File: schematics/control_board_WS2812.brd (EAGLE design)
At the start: 58.4 x 55.9 mm, 48 parts, among them J1 POWER_JACKPTH, U1 ATMEGA168, Y1 16MHZ

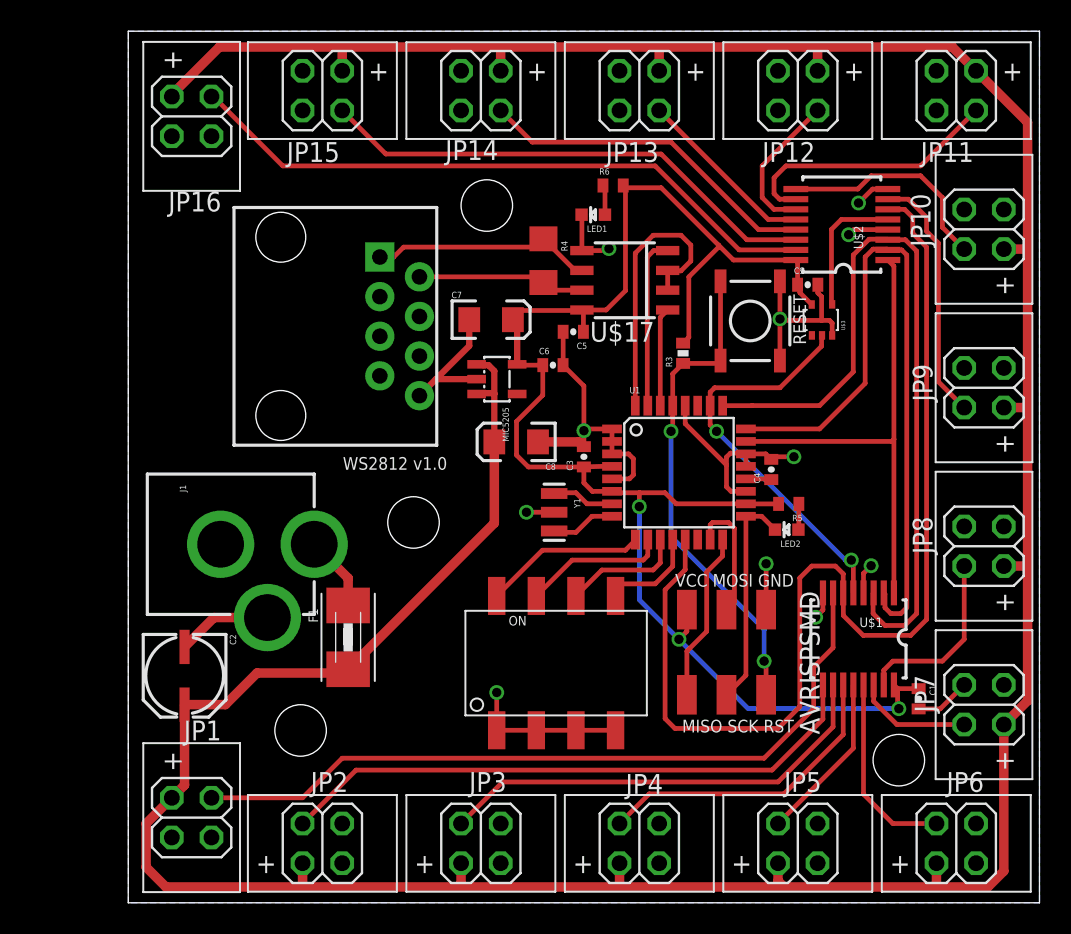
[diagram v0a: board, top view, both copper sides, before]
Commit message: changed WS2812 controller to uUSB, minor spacing edits to everything else
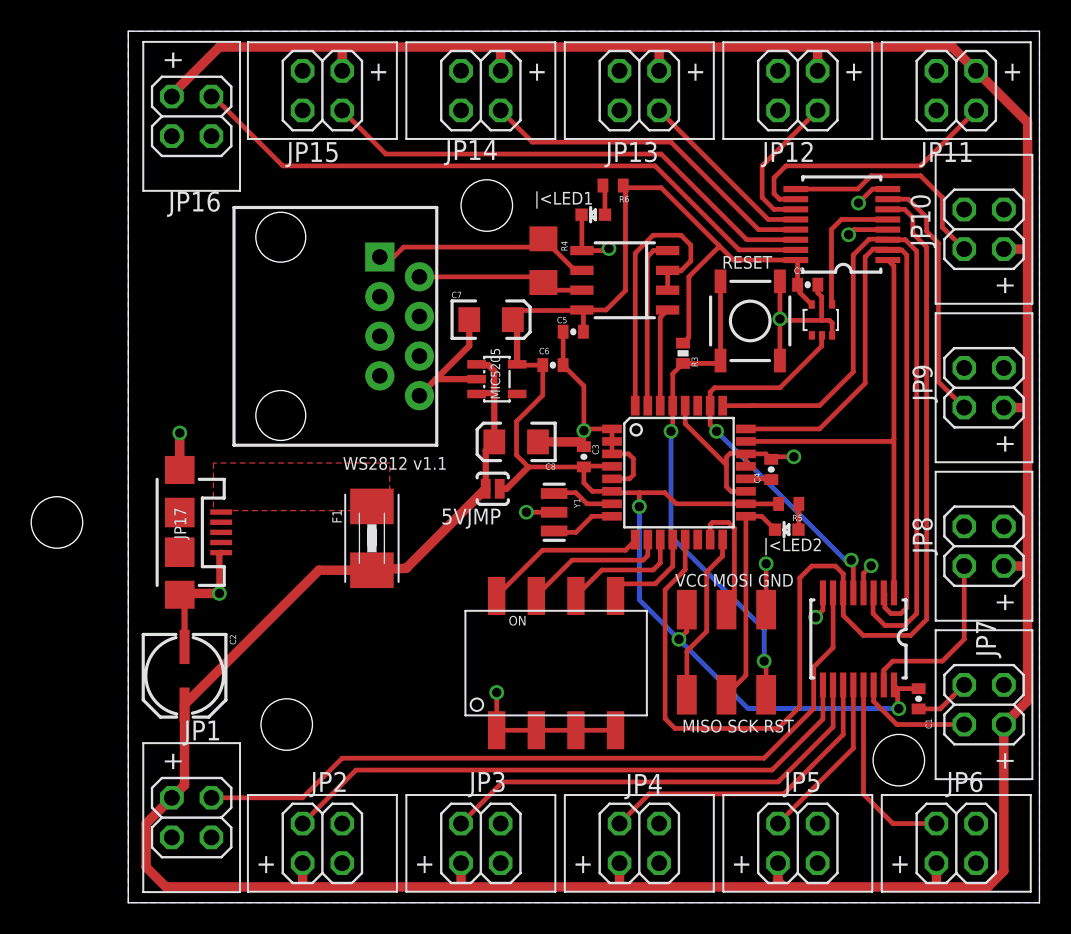
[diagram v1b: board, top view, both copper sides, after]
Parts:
- removed J1: POWER_JACKPTH, SparkFun-Connectors:POWER_JACK_PTH
- added 5VJMP: (no value), SparkFun-Passives:SJ_2S-NO
- added JP17: USB-MICROB, SparkFun-Connectors:USB-MICROB
- moved STANDOFF4 22.9 mm to (-4.32, 24.4)
- moved F1 6.53 mm to (15.9, 23.4)
- moved STANDOFF3 0.97 mm to (10.4, 11.4)
- renumbered LED1 to |<LED1, LED2 to |<LED2
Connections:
- net GND: now also JP17.GND, JP17.MT1, JP17.MT2; no longer J1.GND, J1.GNDBREAK
- net N$8: now also JP17.VBUS; no longer J1.PWR
- net VCC: now also 5VJMP.2
- net VDD: now also 5VJMP.1
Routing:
- net GND: track 90.3 -> 95.3 mm, vias 11 -> 13
- net N$8: track 4.82 -> 0.00 mm
- net VCC: track 102.7 -> 105.1 mm
- net VDD: track 230.0 -> 228.3 mm
- added copper zone on layer 1, net N$8
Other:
- board text added: "WS2812 v1.1"
- board text removed: "WS2812 v1.0"

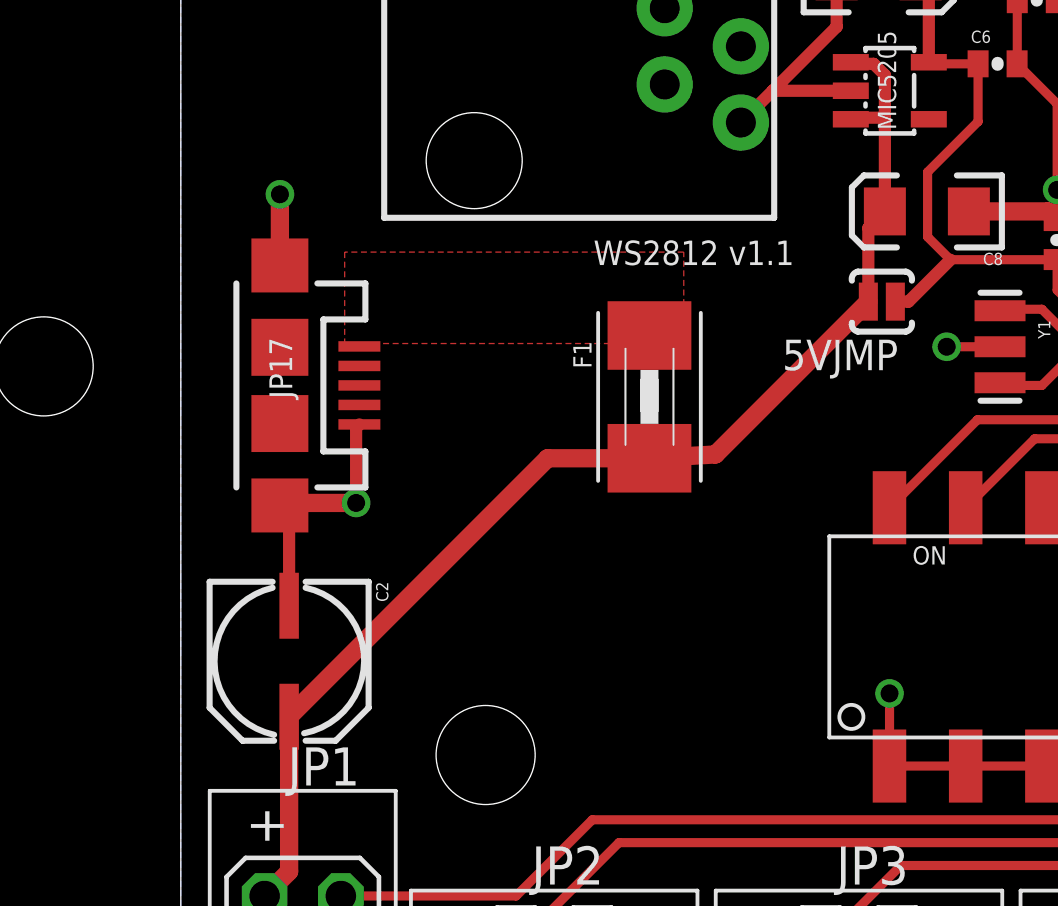
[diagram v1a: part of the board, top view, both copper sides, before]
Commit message: added full ethernet switch board (unfinished), modified WS2812 controller
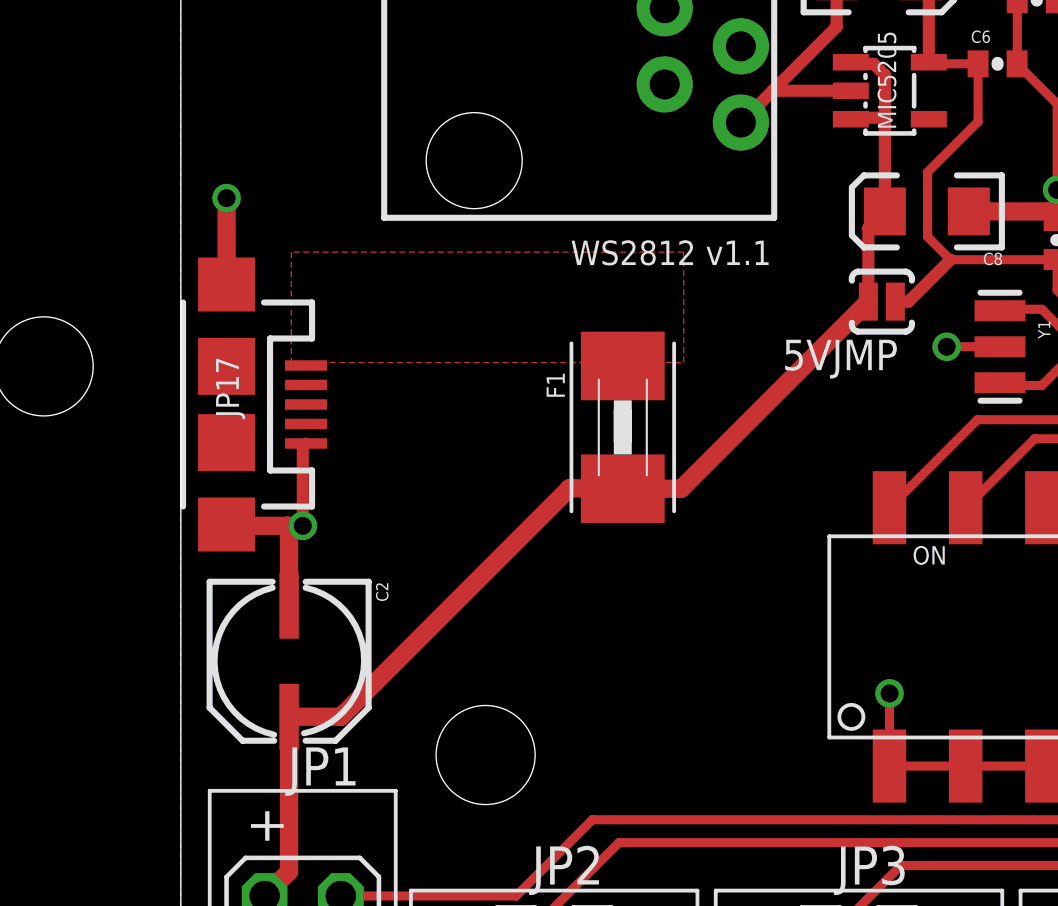
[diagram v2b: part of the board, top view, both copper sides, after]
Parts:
- moved JP17 1.89 mm to (1.78, 23.1)
- moved F1 1.35 mm to (15.0, 22.4)
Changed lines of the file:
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@@
 <wire x1="58.674" y1="55.88" x2="0.254" y2="55.88" width="0" layer="20"/>
 <wire x1="0.254" y1="55.88" x2="0.254" y2="0" width="0" layer="20"/>
-<text x="20.701" y="28.575" size="0.8128" layer="21" ratio="20" distance="213" align="top-right">WS2812 v1.1</text>
+<text x="19.939" y="28.575" size="0.8128" layer="21" ratio="20" distance="213" align="top-right">WS2812 v1.1</text>
 <text x="42.926" y="21.082" size="0.8128" layer="25" ratio="15" distance="130" rot="R180">VCC MOSI GND
 MISO SCK RST</text>
@@
 <attribute name="VALUE" x="43.48660625" y="25.00281875" size="0.4064" layer="27" rot="R180"/>
 </element>
-<element name="F1" library="adafruit" package="1812" value="" x="15.875" y="23.368" rot="R270"/>
+<element name="F1" library="adafruit" package="1812" value="" x="14.986" y="22.352" rot="R270"/>
 <element name="STANDOFF3" library="SparkFun-Electromechanical" package="STAND-OFF" value="STAND-OFF" x="10.414" y="11.43"/>
 <element name="JP1" library="pinhead" package="2X02" value="" x="4.318" y="5.461" smashed="yes" rot="R90">
@@
 <attribute name="VALUE" x="46.303940625" y="34.6950375" size="0.254" layer="27" rot="R90"/>
 </element>
-<element name="JP17" library="SparkFun-Connectors" package="USB-MICROB" value="USB-MICROB" x="3.556" y="23.749" rot="R270">
-<attribute name="PROD_ID" value="CONN-09505" x="3.556" y="23.749" size="1.778" layer="27" rot="R270" display="off"/>
+<element name="JP17" library="SparkFun-Connectors" package="USB-MICROB" value="USB-MICROB" x="1.778" y="23.114" rot="R270">
+<attribute name="PROD_ID" value="CONN-09505" x="1.778" y="23.114" size="1.778" layer="27" rot="R270" display="off"/>
 </element>
 <element name="5VJMP" library="SparkFun-Passives" package="SJ_2S-NO" value="" x="23.622" y="26.543" smashed="yes">
@@
 <contactref element="JP17" pad="MT2"/>
 <contactref element="JP17" pad="MT1"/>
-<wire x1="3.864" y1="16.405" x2="3.864" y2="19.441" width="0.4064" layer="1"/>
-<wire x1="3.864" y1="19.441" x2="3.556" y2="19.749" width="0.4064" layer="1"/>
-<via x="6.09754375" y="19.83224375" extent="1-16" drill="0.6" shape="octagon"/>
-<via x="3.55754375" y="30.11924375" extent="1-16" drill="0.6" shape="octagon"/>
-<wire x1="3.556" y1="27.749" x2="3.556" y2="30.1177" width="0.6096" layer="1"/>
-<wire x1="3.556" y1="30.1177" x2="3.55754375" y2="30.11924375" width="0.6096" layer="1"/>
-<wire x1="6.09754375" y1="19.83224375" x2="3.63924375" y2="19.83224375" width="0.6096" layer="1"/>
-<wire x1="3.63924375" y1="19.83224375" x2="3.556" y2="19.749" width="0.6096" layer="1"/>
-<wire x1="6.09754375" y1="19.83224375" x2="6.09754375" y2="22.34054375" width="0.4064" layer="1"/>
-<wire x1="6.09754375" y1="22.34054375" x2="6.206" y2="22.449" width="0.4064" layer="1"/>
+<via x="4.31954375" y="19.07024375" extent="1-16" drill="0.6" shape="octagon"/>
+<wire x1="4.31954375" y1="19.07024375" x2="3.81" y2="19.07024375" width="0.6096" layer="1"/>
+<wire x1="3.81" y1="19.07024375" x2="1.82175625" y2="19.07024375" width="0.6096" layer="1"/>
+<wire x1="1.82175625" y1="19.07024375" x2="1.778" y2="19.114" width="0.6096" layer="1"/>
+<wire x1="3.864" y1="16.405" x2="3.864" y2="19.01624375" width="0.6096" layer="1"/>
+<wire x1="3.864" y1="19.01624375" x2="3.81" y2="19.07024375" width="0.6096" layer="1"/>
+<wire x1="4.31954375" y1="19.07024375" x2="4.31954375" y2="21.70554375" width="0.4064" layer="1"/>
+<wire x1="4.31954375" y1="21.70554375" x2="4.428" y2="21.814" width="0.4064" layer="1"/>
+<via x="1.77954375" y="29.99224375" extent="1-16" drill="0.6" shape="octagon"/>
+<wire x1="1.77954375" y1="29.99224375" x2="1.77954375" y2="27.11554375" width="0.6096" layer="1"/>
+<wire x1="1.77954375" y1="27.11554375" x2="1.778" y2="27.114" width="0.6096" layer="1"/>
 </signal>
 <signal name="VCC">
@@
 <wire x1="23.172" y1="26.543" x2="23.172" y2="28.998953125" width="0.4064" layer="1"/>
 <wire x1="23.172" y1="28.998953125" x2="23.722659375" y2="29.5496125" width="0.4064" layer="1"/>
-<wire x1="23.172" y1="26.543" x2="18.078" y2="21.449" width="0.6096" layer="1"/>
-<wire x1="18.078" y1="21.449" x2="15.875" y2="21.322" width="0.6096" layer="1"/>
-<wire x1="15.875" y1="21.322" x2="12.481" y2="21.322" width="0.6096" layer="1"/>
-<wire x1="12.481" y1="21.322" x2="3.864" y2="12.705" width="0.6096" layer="1"/>
+<wire x1="23.172" y1="26.543" x2="16.935" y2="20.306" width="0.6096" layer="1"/>
+<wire x1="14.986" y1="20.306" x2="16.935" y2="20.306" width="0.6096" layer="1"/>
+<wire x1="3.864" y1="12.705" x2="5.593" y2="12.705" width="0.6096" layer="1"/>
+<wire x1="5.593" y1="12.705" x2="13.208" y2="20.32" width="0.6096" layer="1"/>
+<wire x1="13.208" y1="20.32" x2="14.972" y2="20.32" width="0.6096" layer="1"/>
+<wire x1="14.972" y1="20.32" x2="14.986" y2="20.306" width="0.6096" layer="1"/>
 </signal>
 <signal name="DATA1+">
@@
 <contactref element="JP17" pad="VBUS"/>
 <polygon width="0.4064" layer="1">
-<vertex x="5.715" y="25.146"/>
-<vertex x="17.018" y="25.146"/>
+<vertex x="3.937" y="24.511"/>
+<vertex x="17.018" y="24.511"/>
 <vertex x="17.018" y="28.194"/>
-<vertex x="5.715" y="28.194"/>
+<vertex x="3.937" y="28.194"/>
 </polygon>
 </signal>

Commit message: minor tweaks
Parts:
- removed STANDOFF4: STAND-OFF, SparkFun-Electromechanical:STAND-OFF
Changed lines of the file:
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@@
 </element>
 <element name="STANDOFF2" library="SparkFun-Electromechanical" package="STAND-OFF" value="STAND-OFF" x="49.657" y="9.144"/>
-<element name="STANDOFF4" library="SparkFun-Electromechanical" package="STAND-OFF" value="STAND-OFF" x="-4.318" y="24.384"/>
 <element name="U$17" library="751xx" package="D_R-PDSO-G8" value="75176B" x="32.087415625" y="39.910365625" smashed="yes" rot="R90">
 <attribute name="VALUE" x="38.564415625" y="43.974365625" size="1.27" layer="27" ratio="15" rot="R180"/>
